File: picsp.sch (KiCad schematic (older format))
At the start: 3 parts, among them J1 Raspberry_Pi_2_3, J2 ICSP10, J3 ICSP6

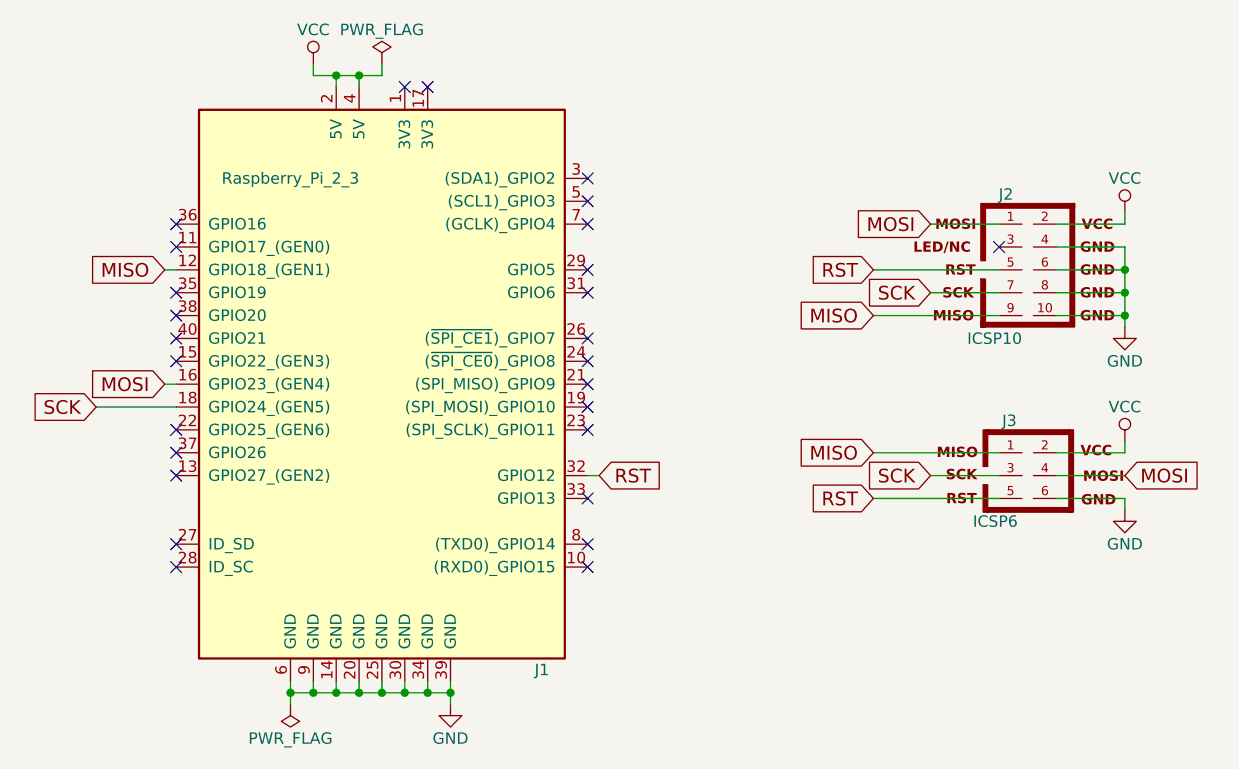
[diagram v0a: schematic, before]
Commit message: Replace AVR-ISP symbols with generic 2.54mm headers
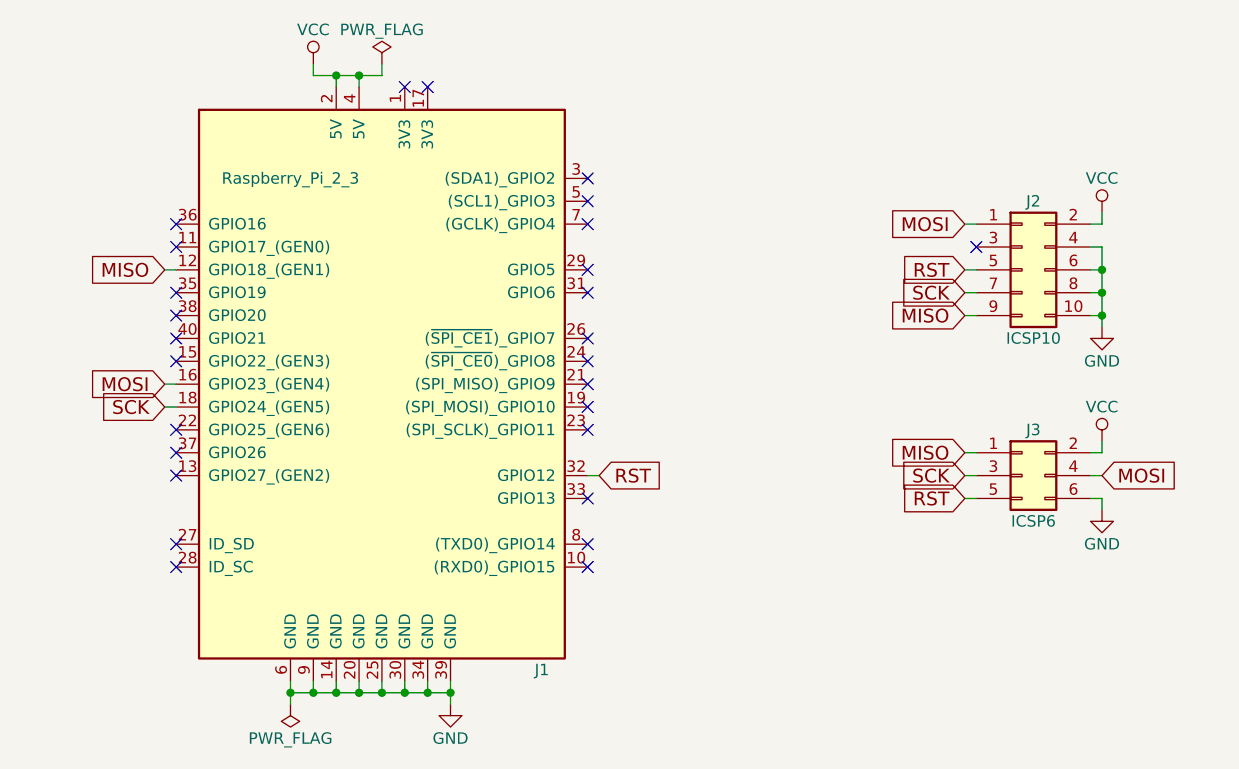
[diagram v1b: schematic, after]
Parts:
- removed J2: ICSP10, Connectors_IDC:IDC-Header_2x05_Pitch2.54mm_Angled, symbol AVR-ISP-10
- removed J3: ICSP6, Connectors_IDC:IDC-Header_2x03_Pitch2.54mm_Angled, symbol AVR-ISP-6
- added J2: ICSP10, Connectors_IDC:IDC-Header_2x05_Pitch2.54mm_Angled, symbol Conn_02x05_Odd_Even
- added J3: ICSP6, Connectors_IDC:IDC-Header_2x03_Pitch2.54mm_Angled, symbol Conn_02x03_Odd_Even
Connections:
- net GND: now also J2.10 (Pin_10), J2.4 (Pin_4), J2.6 (Pin_6), J2.8 (Pin_8), J3.6 (Pin_6)
- net MISO: now also J2.9 (Pin_9), J3.1 (Pin_1)
- net MOSI: now also J2.1 (Pin_1), J3.4 (Pin_4)
- net RST: now also J2.5 (Pin_5), J3.5 (Pin_5)
- net SCK: now also J2.7 (Pin_7), J3.3 (Pin_3)
- net VCC: now also J2.2 (Pin_2), J3.2 (Pin_2)
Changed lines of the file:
@@
 Comment4 "Raspberry Pi ICSP adapter"
 $EndDescr
-NoConn ~ 7450 3050
-$Comp
-L AVR-ISP-10 J2
-U 1 1 59C8D8A3
-P 7650 3150
-F 0 "J2" H 7480 3480 50  0000 C CNN
-F 1 "ICSP10" H 7310 2820 50  0000 L BNN
-F 2 "Connectors_IDC:IDC-Header_2x05_Pitch2.54mm_Angled" V 6900 3200 50  0001 C CNN
-F 3 "" H 7650 3150 50  0001 C CNN
-	1    7650 3150
-	1    0    0    -1
-$EndComp
-Text GLabel 7150 2950 0    60   Input ~ 0
+NoConn ~ 7350 3050
+Text GLabel 7300 2950 0    60   Input ~ 0
 MOSI
 Wire Wire Line
-	7150 2950 7450 2950
-Text GLabel 6900 3150 0    60   Input ~ 0
+	7300 2950 7350 2950
+Text GLabel 7300 3150 0    60   Input ~ 0
 RST
-Text GLabel 7150 3250 0    60   Input ~ 0
+Text GLabel 7300 3250 0    60   Input ~ 0
 SCK
-Text GLabel 6900 3350 0    60   Input ~ 0
+Text GLabel 7300 3350 0    60   Input ~ 0
 MISO
 Wire Wire Line
-	6900 3350 7450 3350
-Wire Wire Line
-	7150 3250 7450 3250
-Wire Wire Line
-	6900 3150 7450 3150
+	7300 3350 7350 3350
+Wire Wire Line
+	7300 3250 7350 3250
+Wire Wire Line
+	7300 3150 7350 3150
 Text GLabel 5700 4050 2    60   Input ~ 0
 RST
 Text GLabel 3800 3650 0    60   Input ~ 0
 MOSI
-Text GLabel 3500 3750 0    60   Input ~ 0
+Text GLabel 3800 3750 0    60   Input ~ 0
 SCK
 Text GLabel 3800 3150 0    60   Input ~ 0
@@
 L GND #PWR03
 U 1 1 59C8E271
-P 8000 3400
-F 0 "#PWR03" H 8000 3150 50  0001 C CNN
-F 1 "GND" H 8000 3250 50  0000 C CNN
-F 2 "" H 8000 3400 50  0001 C CNN
-F 3 "" H 8000 3400 50  0001 C CNN
-	1    8000 3400
+P 7900 3400
+F 0 "#PWR03" H 7900 3150 50  0001 C CNN
+F 1 "GND" H 7900 3250 50  0000 C CNN
+F 2 "" H 7900 3400 50  0001 C CNN
+F 3 "" H 7900 3400 50  0001 C CNN
+	1    7900 3400
 	1    0    0    -1
 $EndComp
@@
 L VCC #PWR04
 U 1 1 59C8E2BD
-P 8000 2900
-F 0 "#PWR04" H 8000 2750 50  0001 C CNN
-F 1 "VCC" H 8000 3050 50  0000 C CNN
-F 2 "" H 8000 2900 50  0001 C CNN
-F 3 "" H 8000 2900 50  0001 C CNN
-	1    8000 2900
-	1    0    0    -1
-$EndComp
-Wire Wire Line
-	7700 2950 8000 2950
-Wire Wire Line
-	7700 3050 8000 3050
-Wire Wire Line
-	8000 3050 8000 3400
-Wire Wire Line
-	7700 3150 8000 3150
-Connection ~ 8000 3150
-Wire Wire Line
-	7700 3250 8000 3250
-Connection ~ 8000 3250
-Wire Wire Line
-	8000 3350 7700 3350
-Connection ~ 8000 3350
-Wire Wire Line
-	8000 2950 8000 2900
-Wire Wire Line
-	3850 3750 3500 3750
+P 7900 2900
+F 0 "#PWR04" H 7900 2750 50  0001 C CNN
+F 1 "VCC" H 7900 3050 50  0000 C CNN
+F 2 "" H 7900 2900 50  0001 C CNN
+F 3 "" H 7900 2900 50  0001 C CNN
+	1    7900 2900
+	1    0    0    -1
+$EndComp
+Wire Wire Line
+	7850 2950 7900 2950
+Wire Wire Line
+	7850 3050 7900 3050
+Wire Wire Line
+	7900 3050 7900 3400
+Wire Wire Line
+	7850 3150 7900 3150
+Connection ~ 7900 3150
+Wire Wire Line
+	7850 3250 7900 3250
+Connection ~ 7900 3250
+Wire Wire Line
+	7900 3350 7850 3350
+Connection ~ 7900 3350
+Wire Wire Line
+	7900 2950 7900 2900
+Wire Wire Line
+	3850 3750 3800 3750
 $Comp
 L PWR_FLAG #FLG05
@@
 Wire Wire Line
 	4750 2300 4750 2250
-$Comp
-L AVR-ISP-6 J3
-U 1 1 59C907B1
-P 7600 4050
-F 0 "J3" H 7495 4290 50  0000 C CNN
-F 1 "ICSP6" H 7335 3820 50  0000 L BNN
-F 2 "Connectors_IDC:IDC-Header_2x03_Pitch2.54mm_Angled" V 7080 4090 50  0001 C CNN
-F 3 "" H 7575 4050 50  0001 C CNN
-	1    7600 4050
-	1    0    0    -1
-$EndComp
-Text GLabel 6900 3950 0    60   Input ~ 0
+Text GLabel 7300 3950 0    60   Input ~ 0
 MISO
-Text GLabel 6900 4150 0    60   Input ~ 0
+Text GLabel 7300 4150 0    60   Input ~ 0
 RST
-Text GLabel 7150 4050 0    60   Input ~ 0
+Text GLabel 7300 4050 0    60   Input ~ 0
 SCK
-Text GLabel 8000 4050 2    60   Input ~ 0
+Text GLabel 7900 4050 2    60   Input ~ 0
 MOSI
 Wire Wire Line
-	8000 4050 7700 4050
-Wire Wire Line
-	7450 4050 7150 4050
-Wire Wire Line
-	6900 3950 7450 3950
-Wire Wire Line
-	6900 4150 7450 4150
+	7900 4050 7850 4050
+Wire Wire Line
+	7350 4050 7300 4050
+Wire Wire Line
+	7300 3950 7350 3950
+Wire Wire Line
+	7300 4150 7350 4150
 $Comp
 L VCC #PWR07
 U 1 1 59C909F1
-P 8000 3900
-F 0 "#PWR07" H 8000 3750 50  0001 C CNN
-F 1 "VCC" H 8000 4050 50  0000 C CNN
-F 2 "" H 8000 3900 50  0001 C CNN
-F 3 "" H 8000 3900 50  0001 C CNN
-	1    8000 3900
-	1    0    0    -1
-$EndComp
-Wire Wire Line
-	7700 3950 8000 3950
-Wire Wire Line
-	8000 3950 8000 3900
+P 7900 3900
+F 0 "#PWR07" H 7900 3750 50  0001 C CNN
+F 1 "VCC" H 7900 4050 50  0000 C CNN
+F 2 "" H 7900 3900 50  0001 C CNN
+F 3 "" H 7900 3900 50  0001 C CNN
+	1    7900 3900
+	1    0    0    -1
+$EndComp
+Wire Wire Line
+	7850 3950 7900 3950
+Wire Wire Line
+	7900 3950 7900 3900
 $Comp
 L GND #PWR08
 U 1 1 59C90A6B
-P 8000 4200
-F 0 "#PWR08" H 8000 3950 50  0001 C CNN
-F 1 "GND" H 8000 4050 50  0000 C CNN
-F 2 "" H 8000 4200 50  0001 C CNN
-F 3 "" H 8000 4200 50  0001 C CNN
-	1    8000 4200
-	1    0    0    -1
-$EndComp
-Wire Wire Line
-	8000 4150 7700 4150
-Wire Wire Line
-	8000 4150 8000 4200
+P 7900 4200
+F 0 "#PWR08" H 7900 3950 50  0001 C CNN
+F 1 "GND" H 7900 4050 50  0000 C CNN
+F 2 "" H 7900 4200 50  0001 C CNN
+F 3 "" H 7900 4200 50  0001 C CNN
+	1    7900 4200
+	1    0    0    -1
+$EndComp
+Wire Wire Line
+	7900 4150 7850 4150
+Wire Wire Line
+	7900 4150 7900 4200
+$Comp
+L Conn_02x03_Odd_Even J3
+U 1 1 59F832CD
+P 7550 4050
+F 0 "J3" H 7600 4250 50  0000 C CNN
+F 1 "ICSP6" H 7600 3850 50  0000 C CNN
+F 2 "Connectors_IDC:IDC-Header_2x03_Pitch2.54mm_Angled" H 7550 4050 50  0001 C CNN
+F 3 "" H 7550 4050 50  0001 C CNN
+	1    7550 4050
+	1    0    0    -1
+$EndComp
+$Comp
+L Conn_02x05_Odd_Even J2
+U 1 1 59F83390
+P 7550 3150
+F 0 "J2" H 7600 3450 50  0000 C CNN
+F 1 "ICSP10" H 7600 2850 50  0000 C CNN
+F 2 "Connectors_IDC:IDC-Header_2x05_Pitch2.54mm_Angled" H 7550 3150 50  0001 C CNN
+F 3 "" H 7550 3150 50  0001 C CNN
+	1    7550 3150
+	1    0    0    -1
+$EndComp
 $EndSCHEMATC

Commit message: Update project to 5.0 RC1
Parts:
- J1: footprint Socket_Strips:Socket_Strip_Straight_2x20_Pitch2.54mm -> Connector_PinHeader_2.54mm:PinHeader_2x20_P2.54mm_Vertical; symbol Raspberry_Pi_2_3 -> Connector_Specialized:Raspberry_Pi_2_3
- J2: footprint Connectors_IDC:IDC-Header_2x05_Pitch2.54mm_Angled -> Connector_IDC:IDC-Header_2x05_P2.54mm_Horizontal; symbol Conn_02x05_Odd_Even -> Connector_Generic:Conn_02x05_Odd_Even
- J3: footprint Connectors_IDC:IDC-Header_2x03_Pitch2.54mm_Angled -> Connector_IDC:IDC-Header_2x03_P2.54mm_Horizontal; symbol Conn_02x03_Odd_Even -> Connector_Generic:Conn_02x03_Odd_Even
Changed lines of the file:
@@
-EESchema Schematic File Version 2
-LIBS:power
-LIBS:device
-LIBS:switches
-LIBS:relays
-LIBS:motors
-LIBS:transistors
-LIBS:conn
-LIBS:linear
-LIBS:regul
-LIBS:74xx
-LIBS:cmos4000
-LIBS:adc-dac
-LIBS:memory
-LIBS:xilinx
-LIBS:microcontrollers
-LIBS:dsp
-LIBS:microchip
-LIBS:analog_switches
-LIBS:motorola
-LIBS:texas
-LIBS:intel
-LIBS:audio
-LIBS:interface
-LIBS:digital-audio
-LIBS:philips
-LIBS:display
-LIBS:cypress
-LIBS:siliconi
-LIBS:opto
-LIBS:atmel
-LIBS:contrib
-LIBS:valves
+EESchema Schematic File Version 4
 LIBS:picsp-cache
-EELAYER 25 0
+EELAYER 26 0
 EELAYER END
 $Descr A4 11693 8268
@@
 Sheet 1 1
 Title "PiCSP"
-Date "2017-10-19"
+Date "2018-02-27"
 Rev "A"
 Comp "fauxpark"
@@
 	5700 4050 5650 4050
 $Comp
-L VCC #PWR01
+L power:VCC #PWR01
 U 1 1 59C8E066
 P 4450 2250
@@
 $EndComp
 $Comp
-L GND #PWR02
+L power:GND #PWR02
 U 1 1 59C8E100
 P 5050 5050
@@
 NoConn ~ 5650 3550
 $Comp
-L GND #PWR03
+L power:GND #PWR03
 U 1 1 59C8E271
 P 7900 3400
@@
 $EndComp
 $Comp
-L VCC #PWR04
+L power:VCC #PWR04
 U 1 1 59C8E2BD
 P 7900 2900
@@
 	7850 3050 7900 3050
 Wire Wire Line
-	7900 3050 7900 3400
+	7900 3050 7900 3150
 Wire Wire Line
 	7850 3150 7900 3150
@@
 	3850 3750 3800 3750
 $Comp
-L PWR_FLAG #FLG05
+L power:PWR_FLAG #FLG05
 U 1 1 59C8E603
 P 4750 2250
@@
 $EndComp
 $Comp
-L PWR_FLAG #FLG06
+L power:PWR_FLAG #FLG06
 U 1 1 59C8E730
 P 4350 5050
@@
 $EndComp
 $Comp
-L Raspberry_Pi_2_3 J1
+L Connector_Specialized:Raspberry_Pi_2_3 J1
 U 1 1 59C8D902
 P 4750 3650
 F 0 "J1" H 5450 2400 50  0000 C CNN
 F 1 "Raspberry_Pi_2_3" H 4350 4550 50  0000 C CNN
-F 2 "Socket_Strips:Socket_Strip_Straight_2x20_Pitch2.54mm" H 5750 4900 50  0001 C CNN
+F 2 "Connector_PinHeader_2.54mm:PinHeader_2x20_P2.54mm_Vertical" H 5750 4900 50  0001 C CNN
 F 3 "" H 4800 3500 50  0001 C CNN
 	1    4750 3650
@@
 $EndComp
 Wire Wire Line
-	4350 4950 4350 5050
-Wire Wire Line
-	4350 5000 5050 5000
-Wire Wire Line
-	5050 4950 5050 5050
+	4350 4950 4350 5000
+Wire Wire Line
+	4350 5000 4450 5000
+Wire Wire Line
+	5050 4950 5050 5000
 Wire Wire Line
 	4950 4950 4950 5000
@@
 	4650 2300 4650 2350
 Wire Wire Line
-	4450 2300 4750 2300
+	4450 2300 4550 2300
 Wire Wire Line
 	4550 2300 4550 2350
@@
 	7300 4150 7350 4150
 $Comp
-L VCC #PWR07
+L power:VCC #PWR07
 U 1 1 59C909F1
 P 7900 3900
@@
 	7900 3950 7900 3900
 $Comp
-L GND #PWR08
+L power:GND #PWR08
 U 1 1 59C90A6B
 P 7900 4200
@@
 	7900 4150 7900 4200
 $Comp
-L Conn_02x03_Odd_Even J3
+L Connector_Generic:Conn_02x03_Odd_Even J3
 U 1 1 59F832CD
 P 7550 4050
 F 0 "J3" H 7600 4250 50  0000 C CNN
 F 1 "ICSP6" H 7600 3850 50  0000 C CNN
-F 2 "Connectors_IDC:IDC-Header_2x03_Pitch2.54mm_Angled" H 7550 4050 50  0001 C CNN
+F 2 "Connector_IDC:IDC-Header_2x03_P2.54mm_Horizontal" H 7550 4050 50  0001 C CNN
 F 3 "" H 7550 4050 50  0001 C CNN
 	1    7550 4050
@@
 $EndComp
 $Comp
-L Conn_02x05_Odd_Even J2
+L Connector_Generic:Conn_02x05_Odd_Even J2
 U 1 1 59F83390
 P 7550 3150
 F 0 "J2" H 7600 3450 50  0000 C CNN
 F 1 "ICSP10" H 7600 2850 50  0000 C CNN
-F 2 "Connectors_IDC:IDC-Header_2x05_Pitch2.54mm_Angled" H 7550 3150 50  0001 C CNN
+F 2 "Connector_IDC:IDC-Header_2x05_P2.54mm_Horizontal" H 7550 3150 50  0001 C CNN
 F 3 "" H 7550 3150 50  0001 C CNN
 	1    7550 3150
 	1    0    0    -1
 $EndComp
+Wire Wire Line
+	7900 3150 7900 3250
+Wire Wire Line
+	7900 3250 7900 3350
+Wire Wire Line
+	7900 3350 7900 3400
+Wire Wire Line
+	4950 5000 5050 5000
+Wire Wire Line
+	4850 5000 4950 5000
+Wire Wire Line
+	4750 5000 4850 5000
+Wire Wire Line
+	4650 5000 4750 5000
+Wire Wire Line
+	4550 5000 4650 5000
+Wire Wire Line
+	4450 5000 4550 5000
+Wire Wire Line
+	5050 5000 5050 5050
+Wire Wire Line
+	4350 5000 4350 5050
+Wire Wire Line
+	4550 2300 4650 2300
+Wire Wire Line
+	4650 2300 4750 2300
 $EndSCHEMATC

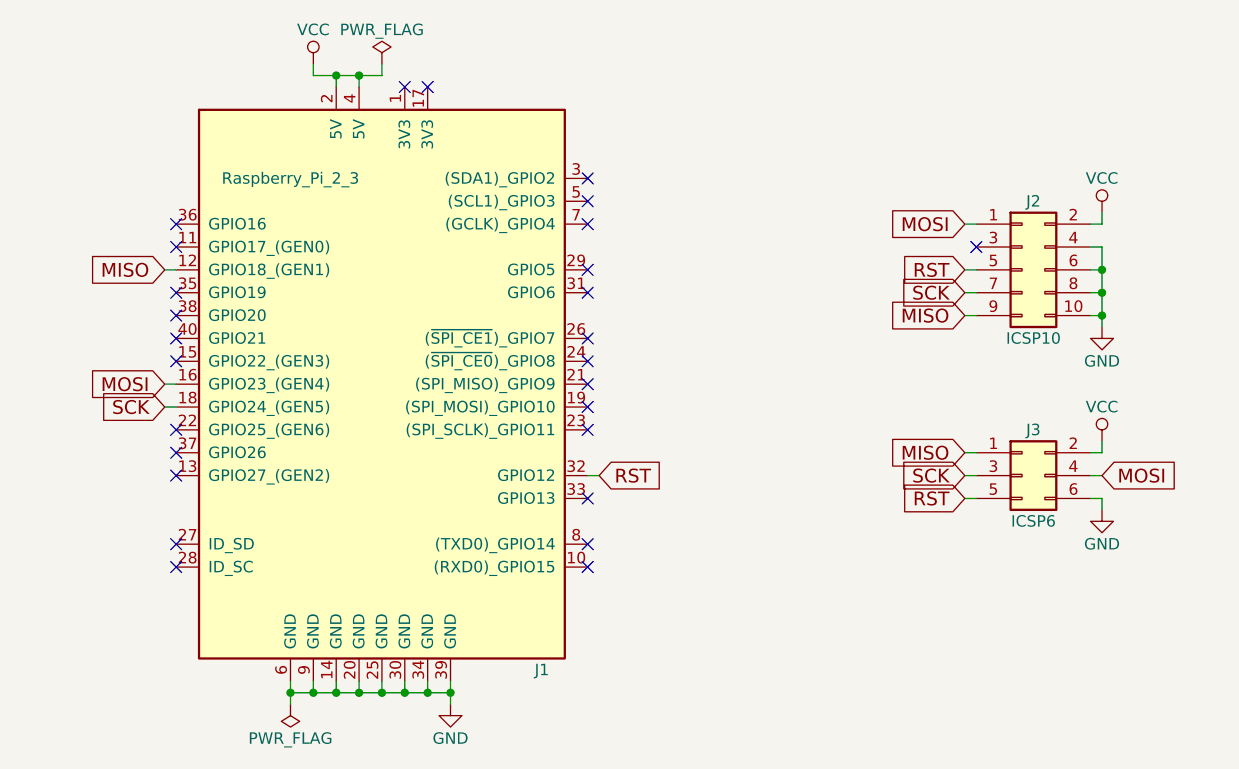
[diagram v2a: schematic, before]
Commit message: Update to use new library symbols
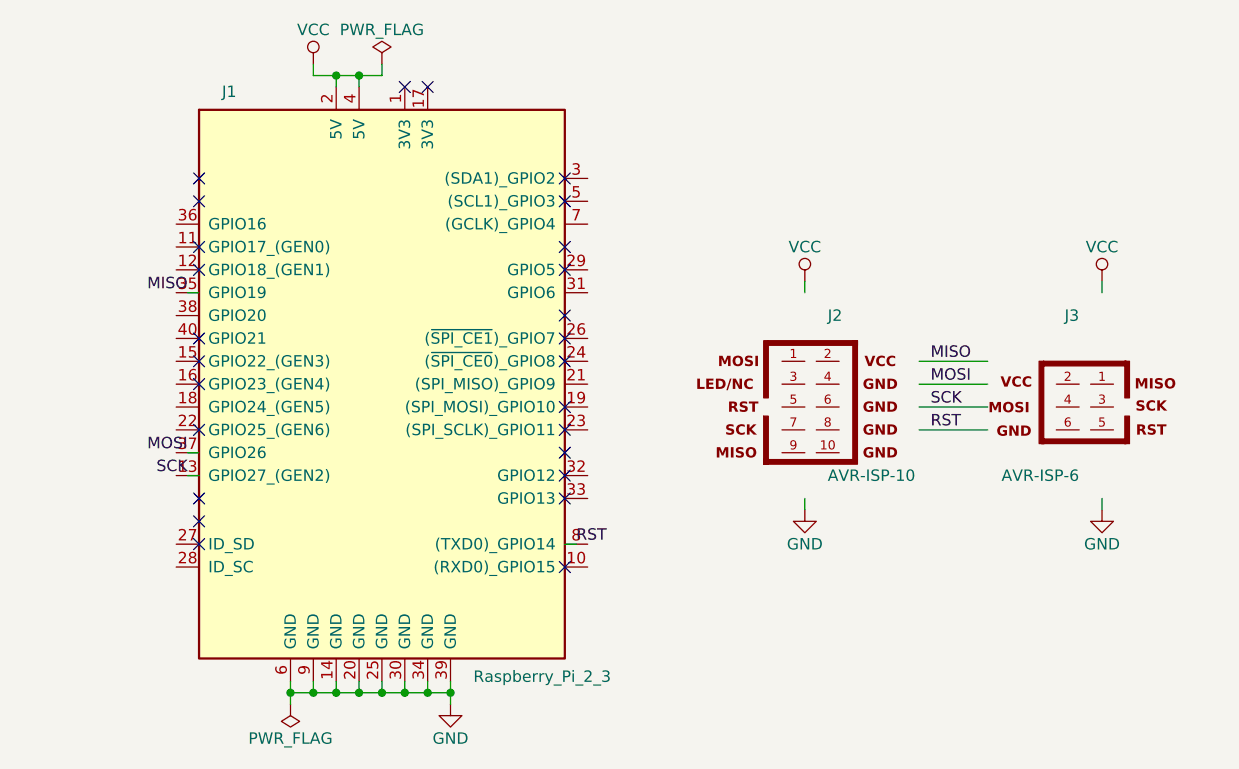
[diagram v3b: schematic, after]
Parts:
- removed J1: Raspberry_Pi_2_3, Connector_PinHeader_2.54mm:PinHeader_2x20_P2.54mm_Vertical, symbol Connector_Specialized:Raspberry_Pi_2_3
- removed J2: ICSP10, Connector_IDC:IDC-Header_2x05_P2.54mm_Horizontal, symbol Connector_Generic:Conn_02x05_Odd_Even
- removed J3: ICSP6, Connector_IDC:IDC-Header_2x03_P2.54mm_Horizontal, symbol Connector_Generic:Conn_02x03_Odd_Even
- added J1: Raspberry_Pi_2_3, Connector_PinSocket_2.54mm:PinSocket_2x20_P2.54mm_Vertical, symbol Connector:Raspberry_Pi_2_3
- added J2: AVR-ISP-10, Connector_IDC:IDC-Header_2x05_P2.54mm_Horizontal, symbol Connector:AVR-ISP-10
- added J3: AVR-ISP-6, Connector_IDC:IDC-Header_2x03_P2.54mm_Horizontal, symbol Connector:AVR-ISP-6
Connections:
- wire segments 50 -> 36
- no-connect marks 27 -> 26
